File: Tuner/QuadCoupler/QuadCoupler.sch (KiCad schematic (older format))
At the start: 109 parts, among them J1 Conn_01x01, J10 Conn_01x02, J11 Conn_01x01, J12 Conn_01x01, J13 Conn_01x01, J14 Conn_01x01, J15 Conn_01x01, J16 Conn_01x01, J17 Conn_01x01, J19 Conn_01x02, J2 Conn_Coaxial, J21 Conn_01x01, J22 Conn_01x01, J23 Conn_01x01, J24 Conn_01x01, J3 Conn_Coaxial, J4 Conn_Coaxial, J5 Conn_Coaxial, J6 Conn_Coaxial, J7 Conn_01x01, J8 Conn_01x01, J9 Conn_01x01

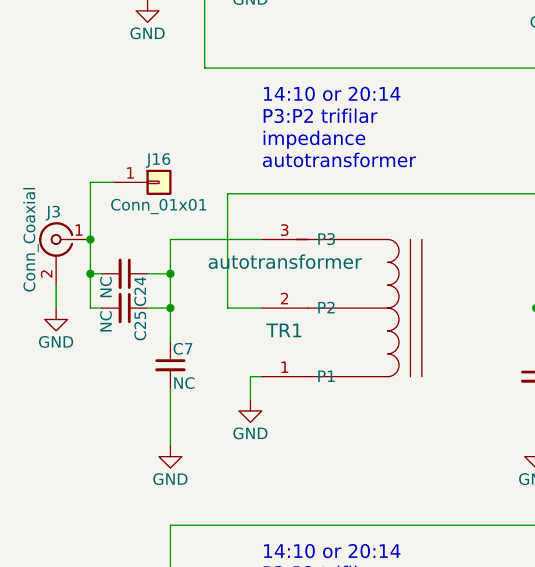
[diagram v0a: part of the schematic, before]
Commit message: Added OptoisolatedRelay
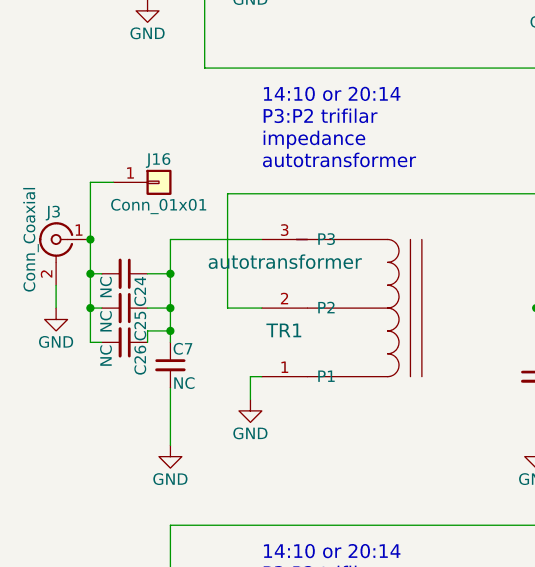
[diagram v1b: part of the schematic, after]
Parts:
- added C26: NC, Capacitors_THT:C_Disc_D5.0mm_W2.5mm_P5.00mm, symbol C_Small
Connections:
- net at C24.2, C25.2, J16.1 (Pin_1)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: now also C26.2
- net at C24.1, C25.1, C7.1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: now also C26.1
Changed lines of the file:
@@
 $EndComp
 $Comp
-L GND #PWR01
+L GND #PWR29
 U 1 1 5C69E7D4
 P 7000 4350
-F 0 "#PWR01" H 7000 4100 50  0001 C CNN
+F 0 "#PWR29" H 7000 4100 50  0001 C CNN
 F 1 "GND" H 7000 4200 50  0000 C CNN
 F 2 "" H 7000 4350 50  0001 C CNN
@@
 $EndComp
 $Comp
-L GND #PWR02
+L GND #PWR7
 U 1 1 5C721A79
 P 1600 4550
-F 0 "#PWR02" H 1600 4300 50  0001 C CNN
+F 0 "#PWR7" H 1600 4300 50  0001 C CNN
 F 1 "GND" H 1600 4400 50  0000 C CNN
 F 2 "" H 1600 4550 50  0001 C CNN
@@
 $EndComp
 $Comp
-L GND #PWR03
+L GND #PWR1
 U 1 1 5C721C63
 P 750 4150
-F 0 "#PWR03" H 750 3900 50  0001 C CNN
+F 0 "#PWR1" H 750 3900 50  0001 C CNN
 F 1 "GND" H 750 4000 50  0000 C CNN
 F 2 "" H 750 4150 50  0001 C CNN
@@
 1:1 bifilar\nautotransformer
 $Comp
-L GND #PWR04
+L GND #PWR6
 U 1 1 5C722D7A
 P 1600 2650
-F 0 "#PWR04" H 1600 2400 50  0001 C CNN
+F 0 "#PWR6" H 1600 2400 50  0001 C CNN
 F 1 "GND" H 1600 2500 50  0000 C CNN
 F 2 "" H 1600 2650 50  0001 C CNN
@@
 1:1 bifilar\nautotransformer
 $Comp
-L GND #PWR05
+L GND #PWR5
 U 1 1 5C722FF5
 P 1550 6500
-F 0 "#PWR05" H 1550 6250 50  0001 C CNN
+F 0 "#PWR5" H 1550 6250 50  0001 C CNN
 F 1 "GND" H 1550 6350 50  0000 C CNN
 F 2 "" H 1550 6500 50  0001 C CNN
@@
 $EndComp
 $Comp
-L GND #PWR06
+L GND #PWR23
 U 1 1 5C723AE4
 P 5750 2050
-F 0 "#PWR06" H 5750 1800 50  0001 C CNN
+F 0 "#PWR23" H 5750 1800 50  0001 C CNN
 F 1 "GND" H 5750 1900 50  0000 C CNN
 F 2 "" H 5750 2050 50  0001 C CNN
@@
 $EndComp
 $Comp
-L GND #PWR07
+L GND #PWR24
 U 1 1 5C72451D
 P 5750 3000
-F 0 "#PWR07" H 5750 2750 50  0001 C CNN
+F 0 "#PWR24" H 5750 2750 50  0001 C CNN
 F 1 "GND" H 5750 2850 50  0000 C CNN
 F 2 "" H 5750 3000 50  0001 C CNN
@@
 $EndComp
 $Comp
-L GND #PWR08
+L GND #PWR26
 U 1 1 5C7248D8
 P 5750 5950
-F 0 "#PWR08" H 5750 5700 50  0001 C CNN
+F 0 "#PWR26" H 5750 5700 50  0001 C CNN
 F 1 "GND" H 5750 5800 50  0000 C CNN
 F 2 "" H 5750 5950 50  0001 C CNN
@@
 $EndComp
 $Comp
-L GND #PWR09
+L GND #PWR27
 U 1 1 5C7248F8
 P 5750 6900
-F 0 "#PWR09" H 5750 6650 50  0001 C CNN
+F 0 "#PWR27" H 5750 6650 50  0001 C CNN
 F 1 "GND" H 5750 6750 50  0000 C CNN
 F 2 "" H 5750 6900 50  0001 C CNN
@@
 $EndComp
 $Comp
-L GND #PWR010
+L GND #PWR18
 U 1 1 5C725A72
 P 5150 3550
-F 0 "#PWR010" H 5150 3300 50  0001 C CNN
+F 0 "#PWR18" H 5150 3300 50  0001 C CNN
 F 1 "GND" H 5150 3400 50  0000 C CNN
 F 2 "" H 5150 3550 50  0001 C CNN
@@
 $EndComp
 $Comp
-L GND #PWR011
+L GND #PWR15
 U 1 1 5C7263A1
 P 4950 3550
-F 0 "#PWR011" H 4950 3300 50  0001 C CNN
+F 0 "#PWR15" H 4950 3300 50  0001 C CNN
 F 1 "GND" H 4950 3400 50  0000 C CNN
 F 2 "" H 4950 3550 50  0001 C CNN
@@
 $EndComp
 $Comp
-L GND #PWR012
+L GND #PWR22
 U 1 1 5C7266C0
 P 5450 3550
-F 0 "#PWR012" H 5450 3300 50  0001 C CNN
+F 0 "#PWR22" H 5450 3300 50  0001 C CNN
 F 1 "GND" H 5450 3400 50  0000 C CNN
 F 2 "" H 5450 3550 50  0001 C CNN
@@
 $EndComp
 $Comp
-L GND #PWR013
+L GND #PWR17
 U 1 1 5C726B07
 P 5050 1500
-F 0 "#PWR013" H 5050 1250 50  0001 C CNN
+F 0 "#PWR17" H 5050 1250 50  0001 C CNN
 F 1 "GND" H 5050 1350 50  0000 C CNN
 F 2 "" H 5050 1500 50  0001 C CNN
@@
 $EndComp
 $Comp
-L GND #PWR014
+L GND #PWR13
 U 1 1 5C726B1E
 P 4850 1500
-F 0 "#PWR014" H 4850 1250 50  0001 C CNN
+F 0 "#PWR13" H 4850 1250 50  0001 C CNN
 F 1 "GND" H 4850 1350 50  0000 C CNN
 F 2 "" H 4850 1500 50  0001 C CNN
@@
 $EndComp
 $Comp
-L GND #PWR015
+L GND #PWR21
 U 1 1 5C726B2C
 P 5350 1500
-F 0 "#PWR015" H 5350 1250 50  0001 C CNN
+F 0 "#PWR21" H 5350 1250 50  0001 C CNN
 F 1 "GND" H 5350 1350 50  0000 C CNN
 F 2 "" H 5350 1500 50  0001 C CNN
@@
 $EndComp
 $Comp
-L GND #PWR016
+L GND #PWR16
 U 1 1 5C728ED4
 P 5000 7450
-F 0 "#PWR016" H 5000 7200 50  0001 C CNN
+F 0 "#PWR16" H 5000 7200 50  0001 C CNN
 F 1 "GND" H 5000 7300 50  0000 C CNN
 F 2 "" H 5000 7450 50  0001 C CNN
@@
 $EndComp
 $Comp
-L GND #PWR017
+L GND #PWR12
 U 1 1 5C728EEB
 P 4800 7450
-F 0 "#PWR017" H 4800 7200 50  0001 C CNN
+F 0 "#PWR12" H 4800 7200 50  0001 C CNN
 F 1 "GND" H 4800 7300 50  0000 C CNN
 F 2 "" H 4800 7450 50  0001 C CNN
@@
 $EndComp
 $Comp
-L GND #PWR018
+L GND #PWR20
 U 1 1 5C728EF9
 P 5300 7450
-F 0 "#PWR018" H 5300 7200 50  0001 C CNN
+F 0 "#PWR20" H 5300 7200 50  0001 C CNN
 F 1 "GND" H 5300 7300 50  0000 C CNN
 F 2 "" H 5300 7450 50  0001 C CNN
@@
 $EndComp
 $Comp
-L GND #PWR019
+L GND #PWR14
 U 1 1 5C729631
 P 4900 5500
-F 0 "#PWR019" H 4900 5250 50  0001 C CNN
+F 0 "#PWR14" H 4900 5250 50  0001 C CNN
 F 1 "GND" H 4900 5350 50  0000 C CNN
 F 2 "" H 4900 5500 50  0001 C CNN
@@
 $EndComp
 $Comp
-L GND #PWR020
+L GND #PWR11
 U 1 1 5C729648
 P 4700 5500
-F 0 "#PWR020" H 4700 5250 50  0001 C CNN
+F 0 "#PWR11" H 4700 5250 50  0001 C CNN
 F 1 "GND" H 4700 5350 50  0000 C CNN
 F 2 "" H 4700 5500 50  0001 C CNN
@@
 $EndComp
 $Comp
-L GND #PWR021
+L GND #PWR19
 U 1 1 5C729656
 P 5200 5500
-F 0 "#PWR021" H 5200 5250 50  0001 C CNN
+F 0 "#PWR19" H 5200 5250 50  0001 C CNN
 F 1 "GND" H 5200 5350 50  0000 C CNN
 F 2 "" H 5200 5500 50  0001 C CNN
@@
 $EndComp
 $Comp
-L GND #PWR022
+L GND #PWR4
 U 1 1 5C74667B
 P 1250 4750
-F 0 "#PWR022" H 1250 4500 50  0001 C CNN
+F 0 "#PWR4" H 1250 4500 50  0001 C CNN
 F 1 "GND" H 1250 4600 50  0000 C CNN
 F 2 "" H 1250 4750 50  0001 C CNN
@@
 $EndComp
 $Comp
-L GND #PWR023
+L GND #PWR8
 U 1 1 5C747152
 P 2850 4750
-F 0 "#PWR023" H 2850 4500 50  0001 C CNN
+F 0 "#PWR8" H 2850 4500 50  0001 C CNN
 F 1 "GND" H 2850 4600 50  0000 C CNN
 F 2 "" H 2850 4750 50  0001 C CNN
@@
 $EndComp
 $Comp
-L GND #PWR024
+L GND #PWR3
 U 1 1 5C747AA2
 P 1150 2800
-F 0 "#PWR024" H 1150 2550 50  0001 C CNN
+F 0 "#PWR3" H 1150 2550 50  0001 C CNN
 F 1 "GND" H 1150 2650 50  0000 C CNN
 F 2 "" H 1150 2800 50  0001 C CNN
@@
 $EndComp
 $Comp
-L GND #PWR025
+L GND #PWR2
 U 1 1 5C748095
 P 1000 6750
-F 0 "#PWR025" H 1000 6500 50  0001 C CNN
+F 0 "#PWR2" H 1000 6500 50  0001 C CNN
 F 1 "GND" H 1000 6600 50  0000 C CNN
 F 2 "" H 1000 6750 50  0001 C CNN
@@
 $EndComp
 $Comp
-L GND #PWR026
+L GND #PWR9
 U 1 1 5C748BEC
 P 2850 6700
-F 0 "#PWR026" H 2850 6450 50  0001 C CNN
+F 0 "#PWR9" H 2850 6450 50  0001 C CNN
 F 1 "GND" H 2850 6550 50  0000 C CNN
 F 2 "" H 2850 6700 50  0001 C CNN
@@
 $EndComp
 $Comp
-L GND #PWR027
+L GND #PWR10
 U 1 1 5C749558
 P 2900 2750
-F 0 "#PWR027" H 2900 2500 50  0001 C CNN
+F 0 "#PWR10" H 2900 2500 50  0001 C CNN
 F 1 "GND" H 2900 2600 50  0000 C CNN
 F 2 "" H 2900 2750 50  0001 C CNN
@@
 $EndComp
 $Comp
-L GND #PWR028
+L GND #PWR28
 U 1 1 5C7B1635
 P 5850 1300
-F 0 "#PWR028" H 5850 1050 50  0001 C CNN
+F 0 "#PWR28" H 5850 1050 50  0001 C CNN
 F 1 "GND" H 5850 1150 50  0000 C CNN
 F 2 "" H 5850 1300 50  0001 C CNN
@@
 $EndComp
 $Comp
-L GND #PWR029
+L GND #PWR25
 U 1 1 5C7B20CD
 P 5750 5000
-F 0 "#PWR029" H 5750 4750 50  0001 C CNN
+F 0 "#PWR25" H 5750 4750 50  0001 C CNN
 F 1 "GND" H 5750 4850 50  0000 C CNN
 F 2 "" H 5750 5000 50  0001 C CNN
@@
 	750  4150 750  4050
 Wire Wire Line
-	900  3600 900  4150
+	900  3600 900  4300
 Connection ~ 7000 4050
 Connection ~ 7000 3750
@@
 	8450 1200 8550 1200
 $Comp
-L GND #PWR030
+L GND #PWR31
 U 1 1 5C7E60AE
 P 8450 1850
-F 0 "#PWR030" H 8450 1600 50  0001 C CNN
+F 0 "#PWR31" H 8450 1600 50  0001 C CNN
 F 1 "GND" H 8450 1700 50  0000 C CNN
 F 2 "" H 8450 1850 50  0001 C CNN
@@
 	8000 2100 8000 2000
 $Comp
-L GND #PWR031
+L GND #PWR30
 U 1 1 5C7E92D6
 P 8100 2200
-F 0 "#PWR031" H 8100 1950 50  0001 C CNN
+F 0 "#PWR30" H 8100 1950 50  0001 C CNN
 F 1 "GND" H 8100 2050 50  0000 C CNN
 F 2 "" H 8100 2200 50  0001 C CNN
@@
 Wire Wire Line
 	1450 6100 1650 6100
+$Comp
+L C_Small C26
+U 1 1 5CB128AF
+P 1050 4300
+F 0 "C26" H 1060 4370 50  0000 L CNN
+F 1 "NC" H 1060 4220 50  0000 L CNN
+F 2 "Capacitors_THT:C_Disc_D5.0mm_W2.5mm_P5.00mm" H 1050 4300 50  0001 C CNN
+F 3 "" H 1050 4300 50  0001 C CNN
+	1    1050 4300
+	0    1    1    0
+$EndComp
+Wire Wire Line
+	1150 4300 1150 4250
+Wire Wire Line
+	1150 4250 1250 4250
+Connection ~ 1250 4250
+Wire Wire Line
+	900  4300 950  4300
+Connection ~ 900  4150
 $EndSCHEMATC

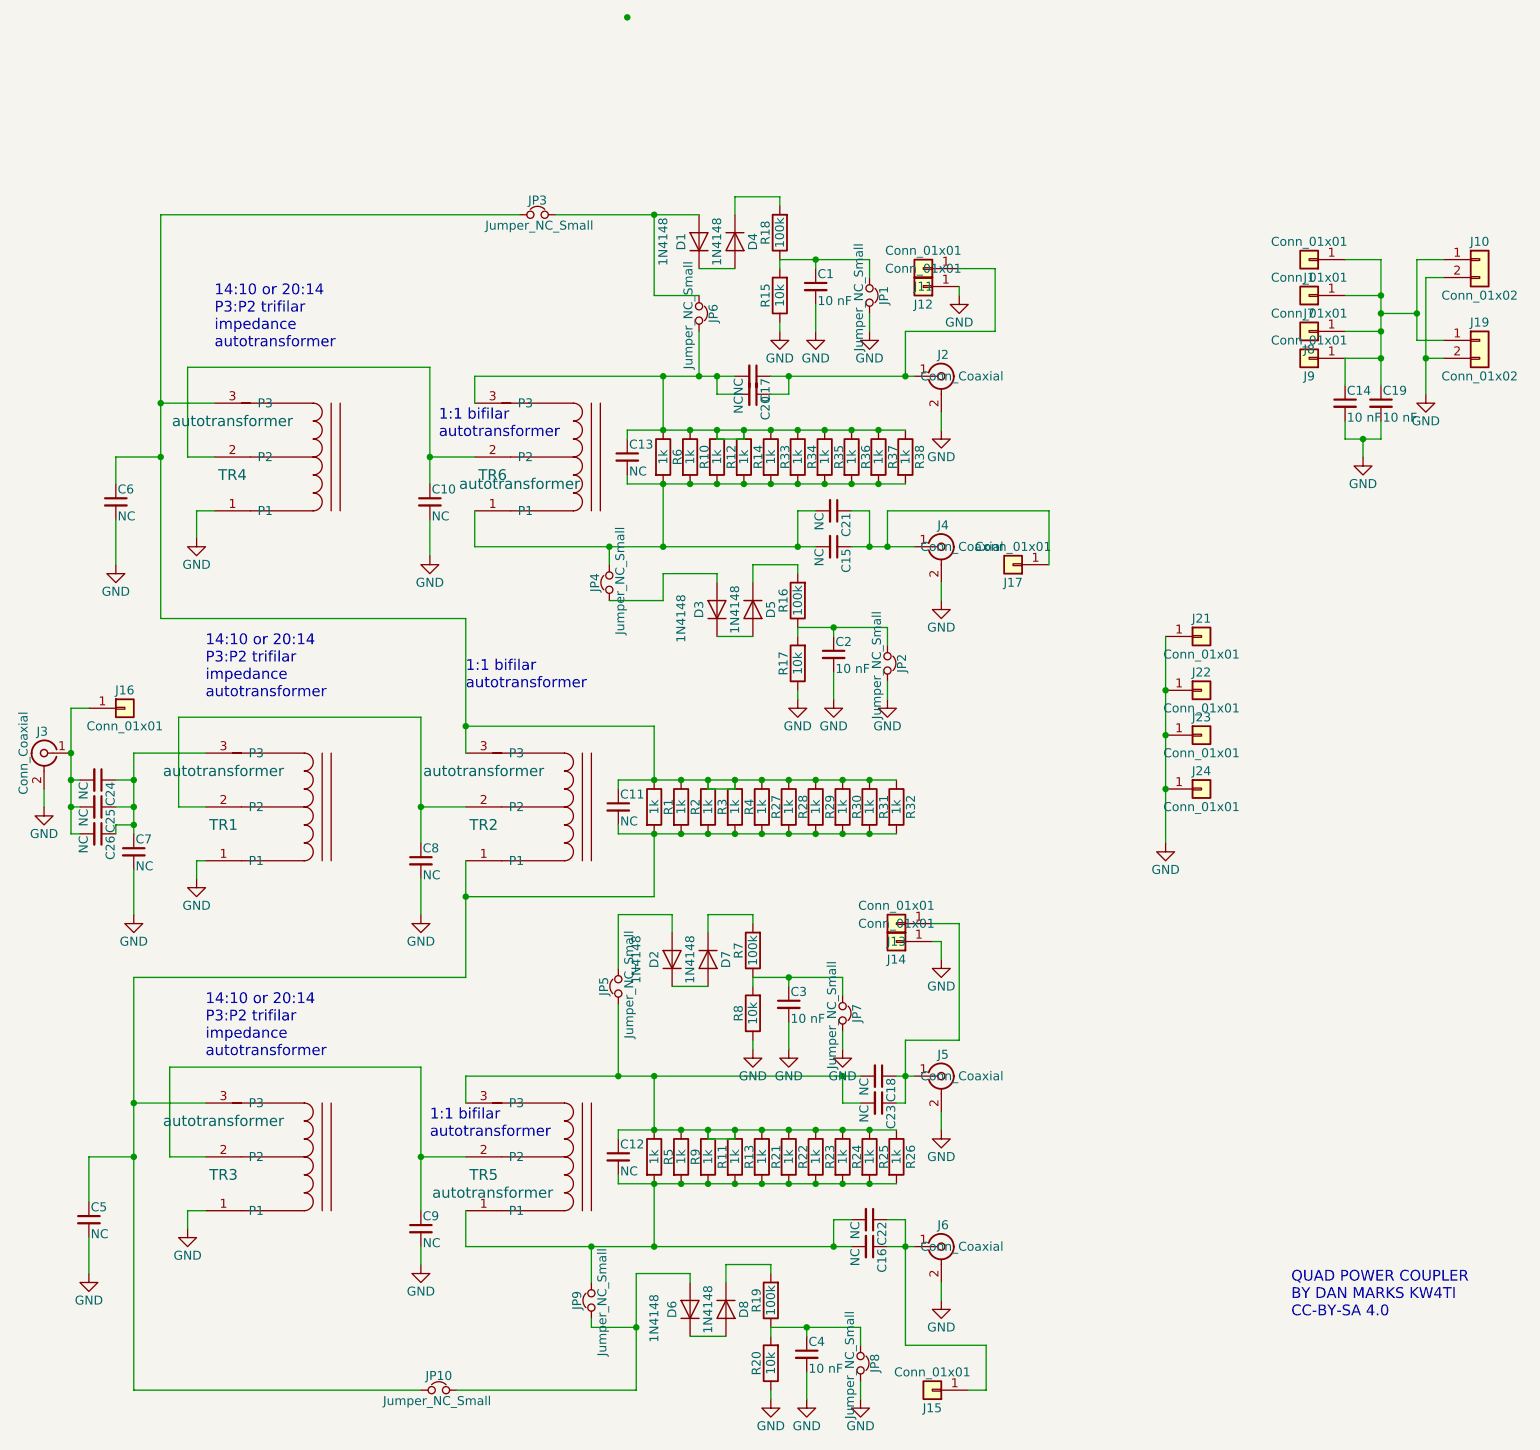
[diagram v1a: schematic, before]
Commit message: Some modifications to Quadcoupler for easier access
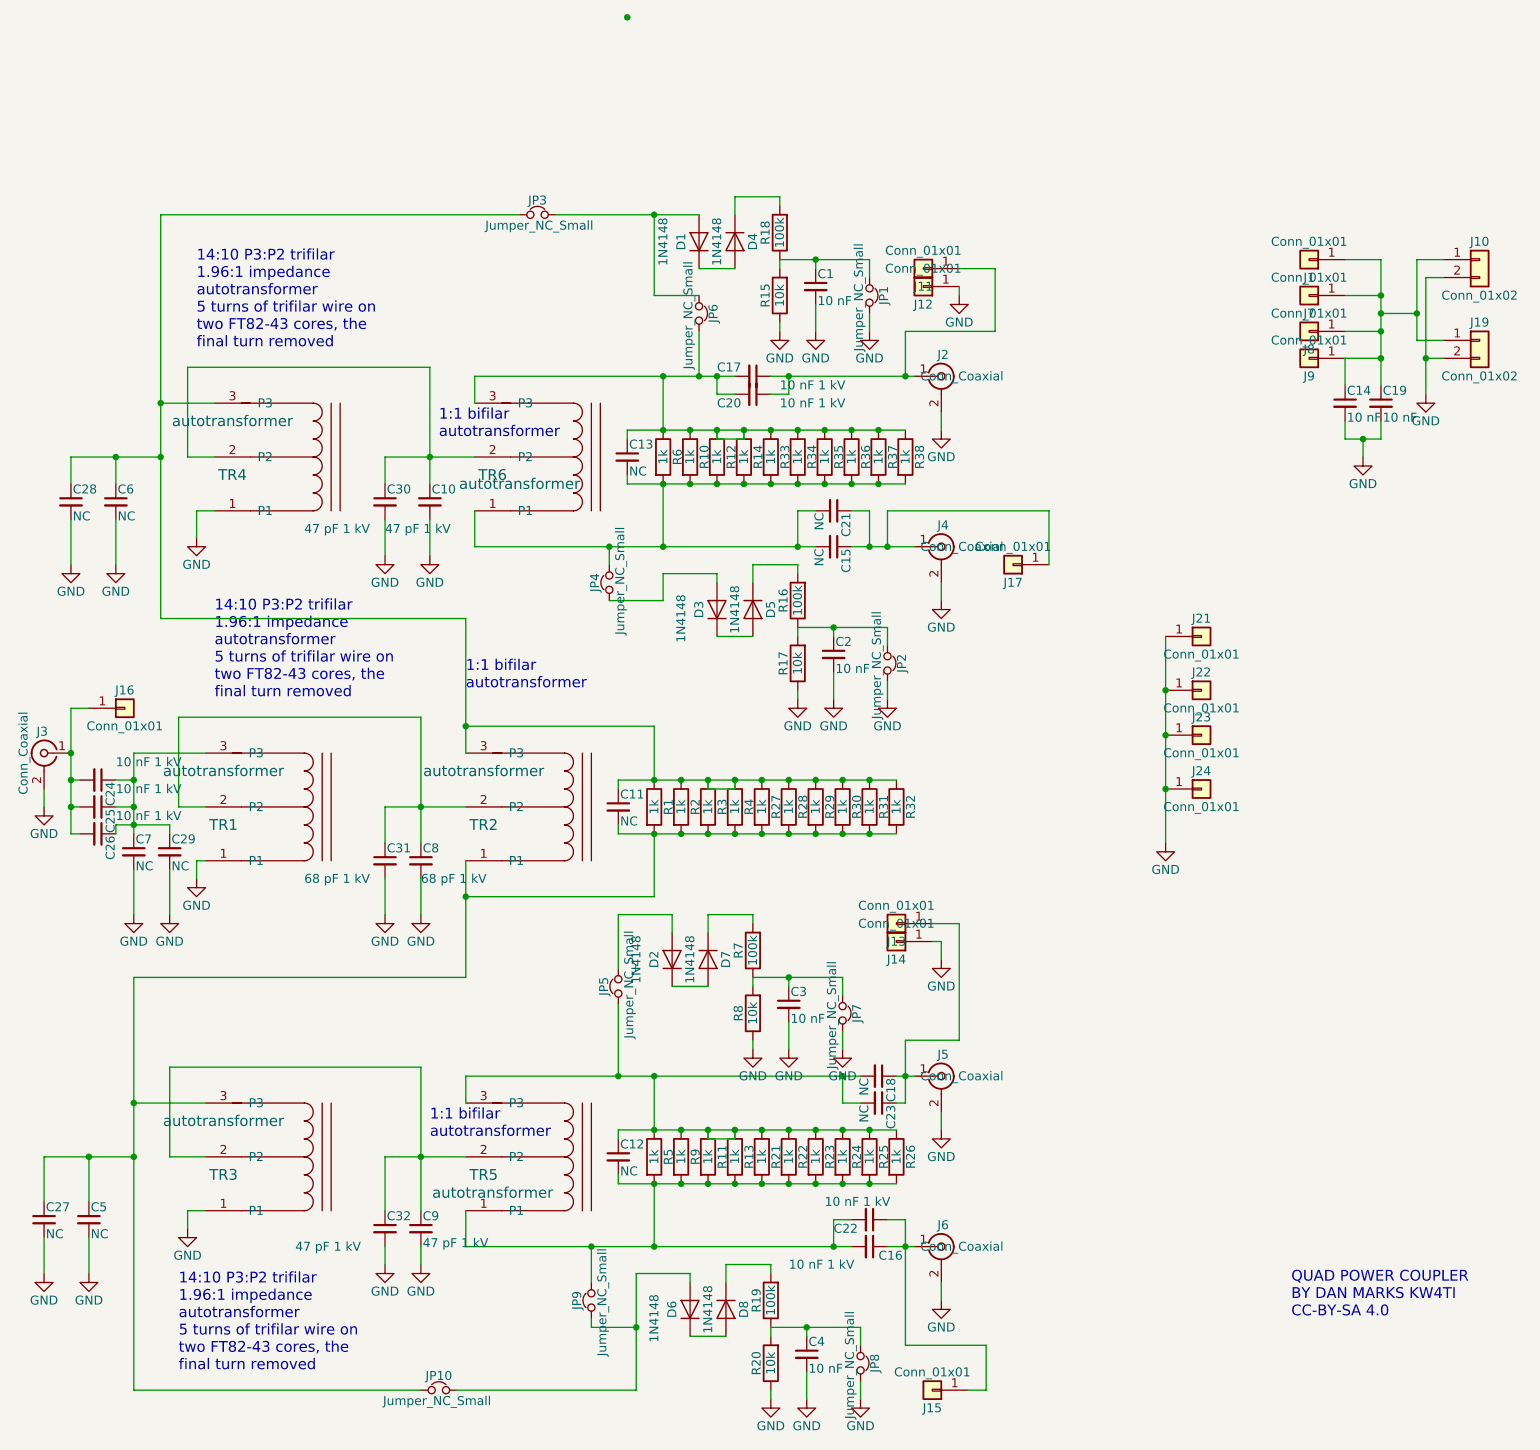
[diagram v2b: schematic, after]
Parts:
- added C27, C28, C29: NC, Capacitors_THT:C_Disc_D5.0mm_W2.5mm_P5.00mm, symbol C_Small
- added C30, C32: 47 pF 1 kV, Capacitors_THT:C_Disc_D5.0mm_W2.5mm_P5.00mm, symbol C_Small
- added C31: 68 pF 1 kV, Capacitors_THT:C_Disc_D5.0mm_W2.5mm_P5.00mm, symbol C_Small
- C10, C9: value NC -> 47 pF 1 kV
- C16, C17, C20, C22, C24, C25, C26: value NC -> 10 nF 1 kV
- C8: value NC -> 68 pF 1 kV
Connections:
- net GND: now also C27.2, C28.2, C29.2, C30.2, C31.2, C32.2
- net at C8.1, TR1.2 (P2), TR2.2 (P2): now also C31.1
- net at C24.1, C25.1, C26.1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: now also C29.1
- net at C11.2, C5.1, JP10.2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: now also C27.1
- net at C11.1, C6.1, JP3.1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: now also C28.1
- net at C10.1, TR4.2 (P2), TR6.2 (P2): now also C30.1
- net at C9.1, TR3.2 (P2), TR5.2 (P2): now also C32.1
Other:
- note added: "14:10 P3:P2 trifilar\n1.96:1 impedance\nautotransformer\n5 turns of trifilar wire on\ntwo FT82-43 cores, the\nfinal turn removed"
- note removed: "14:10 or 20:14 \nP3:P2 trifilar\nimpedance\nautotransformer"
